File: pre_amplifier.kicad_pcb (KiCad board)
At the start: 2 copper layers, 60 x 100 mm, 29 parts, among them J1 AudioJack3_Switch, J2 AudioJack3_Switch, P1 BATT_JACK, P2 CONN_2X1, U1 TL061

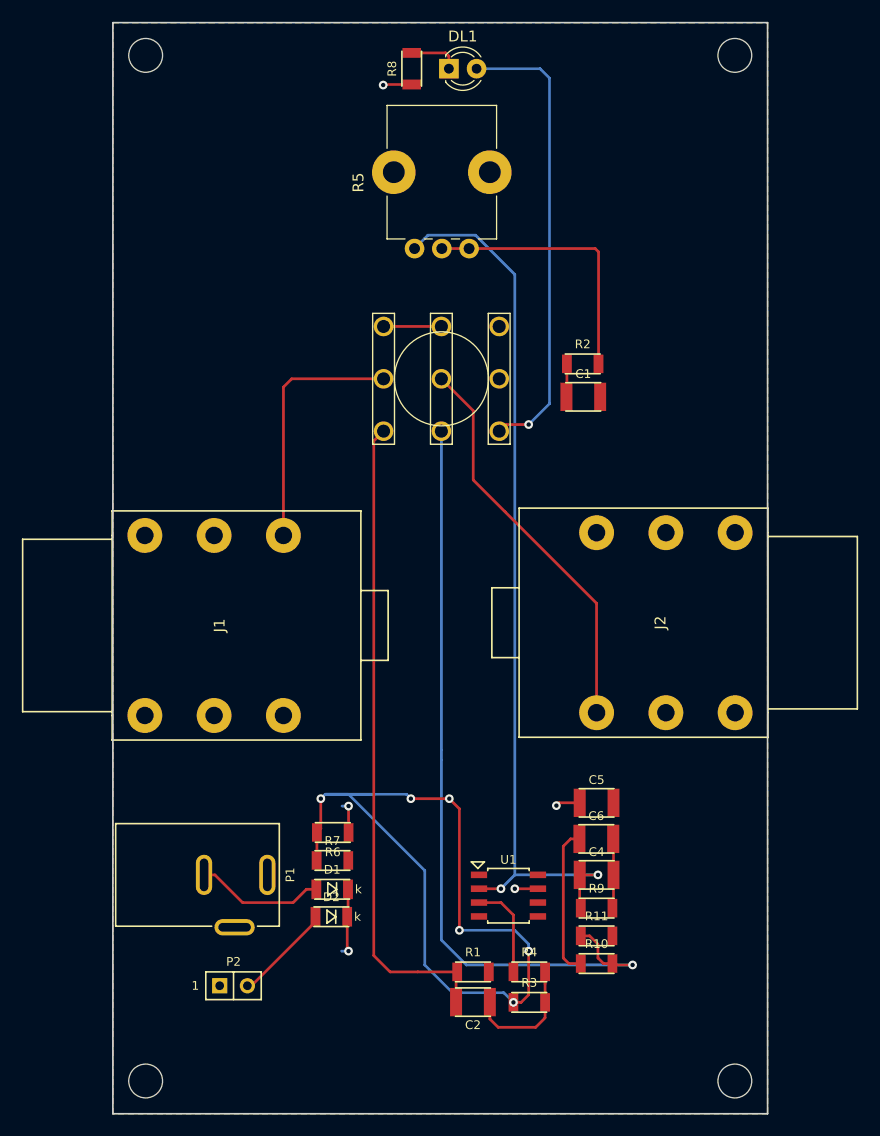
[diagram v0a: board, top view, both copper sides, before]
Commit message: Fixed PCB with changed footprints
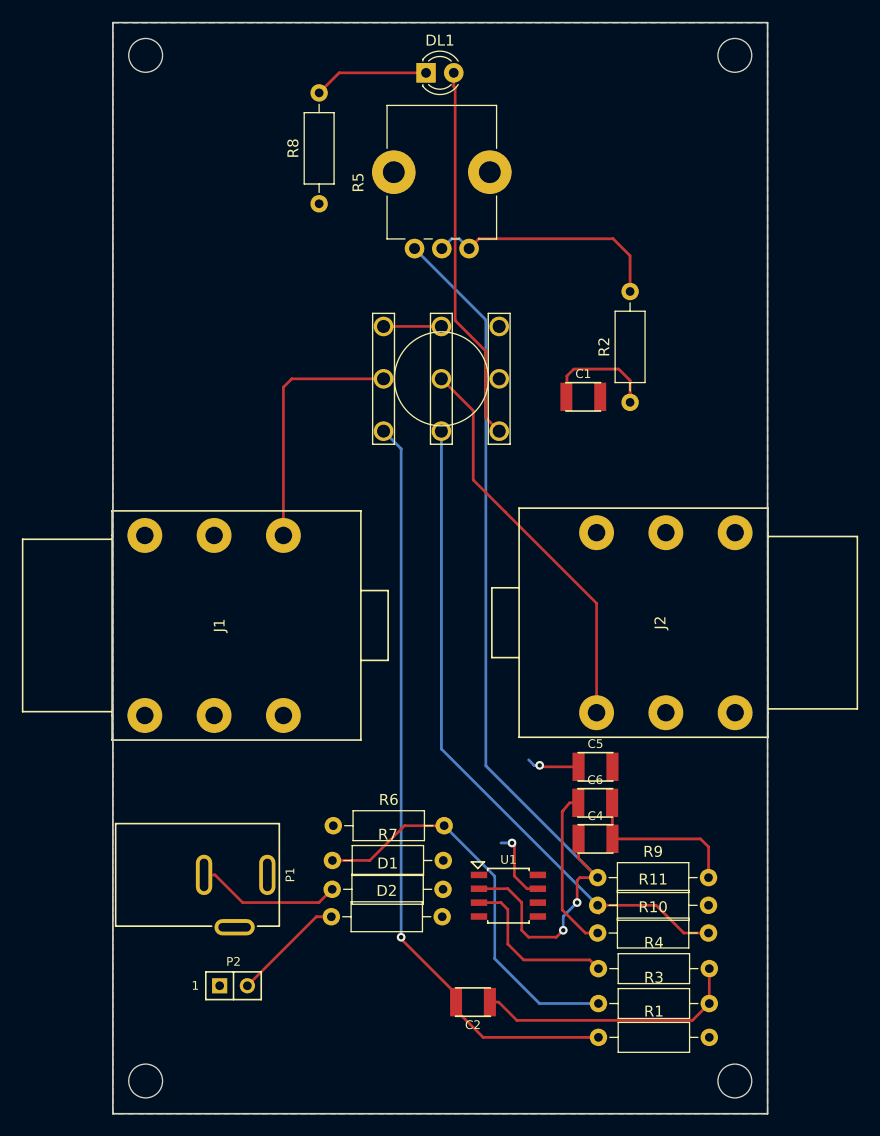
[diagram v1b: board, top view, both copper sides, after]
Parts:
- D1, D2: footprint DIODE:DIODE-1206 -> Resistor_THT:R_Axial_DIN0207_L6.3mm_D2.5mm_P10.16mm_Horizontal
- J1, J2: footprint progetto_delta:CL12327 -> pre_amplifier:CL12327
- R1, R10, R11, R2, R3, R4, R6, R7, R8, R9: footprint RESISTOR:RESISTOR-1206 -> Resistor_THT:R_Axial_DIN0207_L6.3mm_D2.5mm_P10.16mm_Horizontal
- moved R8 15.0 mm to (58.9, 56.6)
- moved R1 13.0 mm to (84.5, 133.0)
- moved R4 6.35 mm to (84.5, 126.7)
- moved R3 6.34 mm to (84.5, 129.9)
- moved R2 5.59 mm to (87.4, 74.8), turned to 90 degrees
- moved C6 3.30 mm to (84.2, 111.5)
- moved C4 3.30 mm to (84.2, 114.8)
- moved C5 3.30 mm to (84.2, 108.2)
- moved R10 2.80 mm to (84.4, 123.4)
- moved R11 2.80 mm to (84.4, 120.9)
- moved R9 2.80 mm to (84.4, 118.4)
- moved DL1 2.12 mm to (68.7, 44.6)
- moved R6 0.63 mm to (60.2, 113.6), turned to 0 degrees
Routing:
- net /4V5: track 78.1 -> 36.9 mm, vias 6 -> 0
- net Net-(C2-Pad1): track 11.5 -> 24.6 mm
- net /sgnIN: track 59.5 -> 69.9 mm, vias 0 -> 1
- net /sgnOUT: track 71.7 -> 61.7 mm, vias 1 -> 0
- net Net-(C4-Pad2): track 6.40 -> 15.2 mm
- net /led-: track 42.5 -> 34.6 mm, vias 1 -> 0
- net Net-(C1-Pad1): track 3.04 -> 10.4 mm
- net Net-(R4-Pad1): track 8.84 -> 15.3 mm
- net Net-(DL1-Pad1): track 4.68 -> 10.6 mm
- net Net-(C4-Pad1): track 82.4 -> 87.3 mm
- net +V: track 16.4 -> 11.6 mm, vias 5 -> 2
- net Net-(R2-Pad2): track 24.8 -> 22.3 mm
- net Net-(D1-Pad1): track 11.9 -> 13.3 mm
- net Net-(C6-Pad1): track 13.8 -> 15.1 mm
- net +VBAT: track 9.13 -> 10.3 mm
